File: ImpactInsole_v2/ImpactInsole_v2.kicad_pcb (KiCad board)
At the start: 2 copper layers, 52.1 x 44.3 mm, 44 parts, among them J1 SFW18R-1STE1LF, J2 Conn_01x02, J3 USB_C_Receptacle_USB2.0_16P, J4 Conn_01x04, SW1 SW_Push, U1 CD74HC4067SM96, U2 TLV9001IDBVR, U3 MCP3201T-CI_SN, U4 LSM6DSOXTR, U5 BQ24075RGTR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

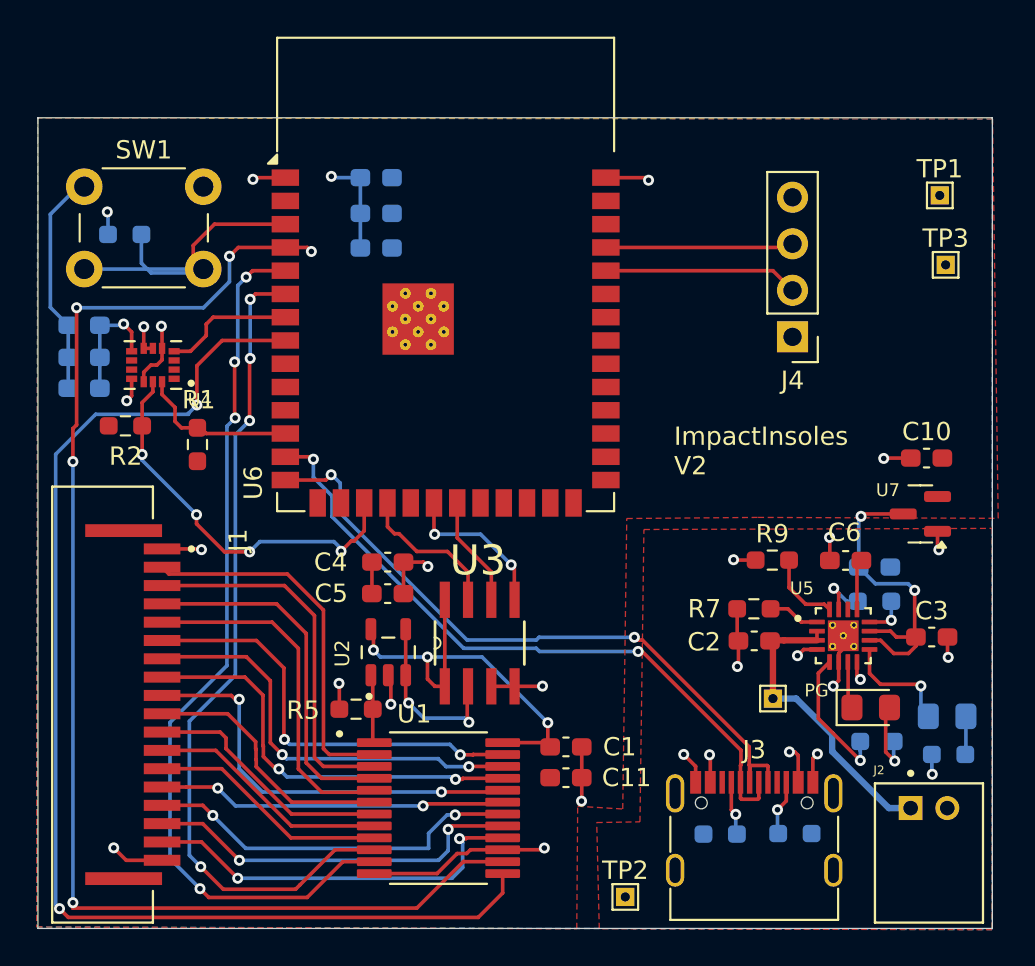
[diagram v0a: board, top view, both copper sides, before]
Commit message: updated silkscreens - sent for round 3
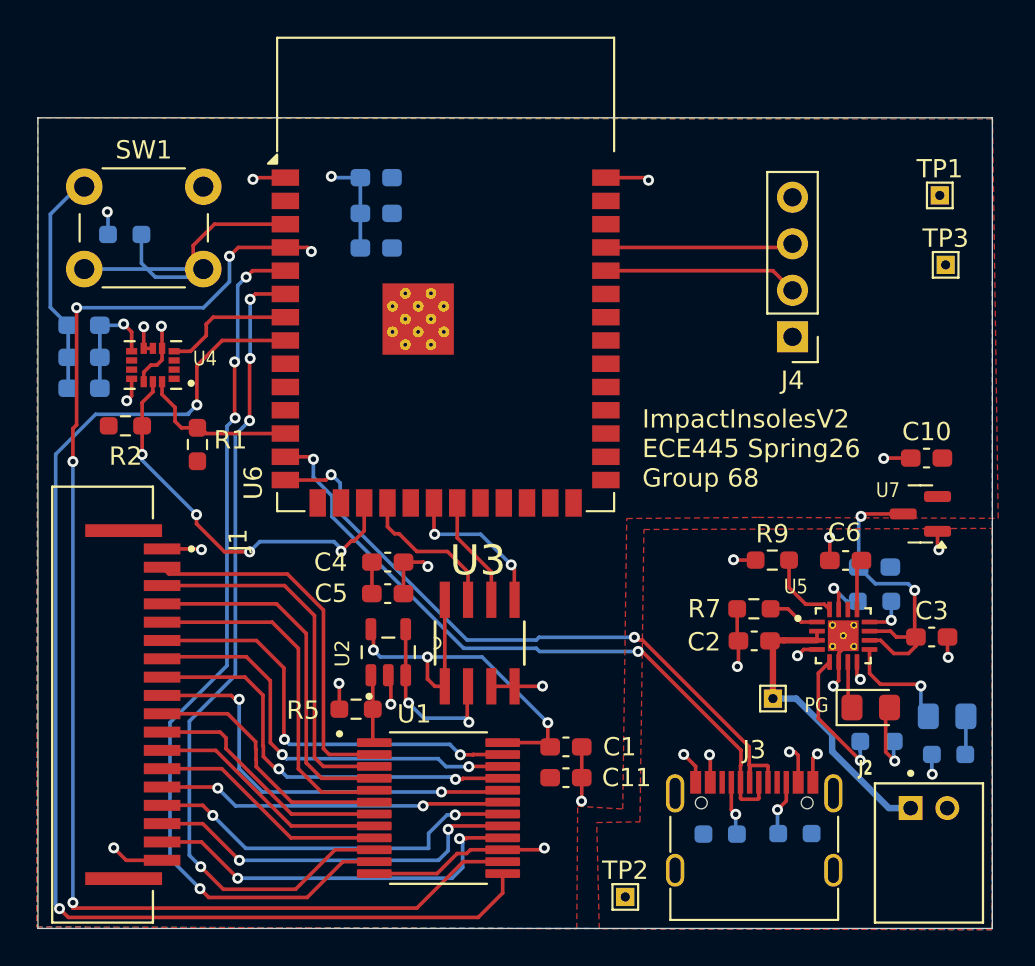
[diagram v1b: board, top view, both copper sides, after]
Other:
- board text added: "ImpactInsolesV2 ECE445 Spring26 Group 68"
- board text removed: "ImpactInsoles V2"
